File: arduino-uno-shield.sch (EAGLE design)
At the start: 28 parts, among them T1 BC547, T2 BC547, T3 BC547, T4 BC547, T5 BC547, T6 BC547, T7 BC547, U1 SN74HC595N

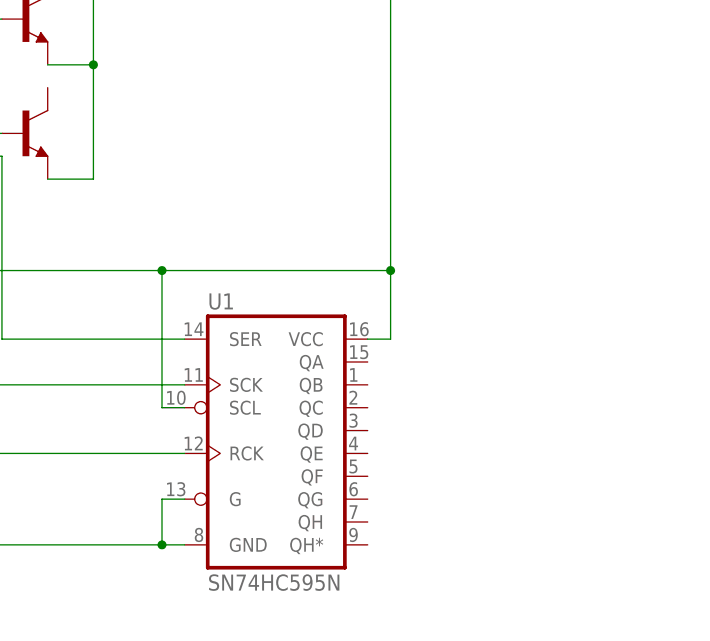
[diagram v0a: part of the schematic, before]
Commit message: Added 6 leds for the clock
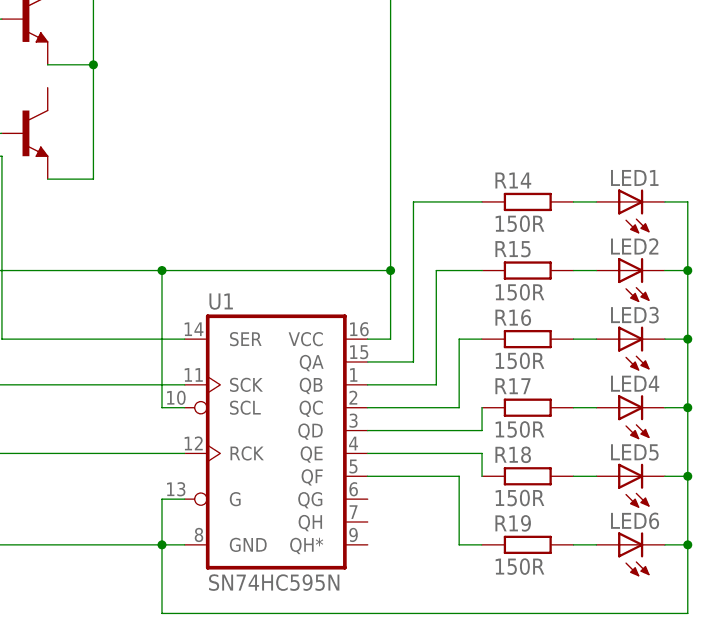
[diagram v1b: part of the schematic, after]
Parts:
- added LED1, LED2, LED3, LED4, LED5, LED6: (no value), led:LED5MM
- added R14, R15, R16, R17, R18, R19: 150R, rcl:R-EU_0204/5
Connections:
- new net N$21: R14.1, U1.QA
- new net N$25: R15.1, U1.QB
- new net N$26: R16.1, U1.QC
- new net N$27: R17.1, U1.QD
- new net N$28: R18.1, U1.QE
- new net N$29: R19.1, U1.QF
- new net N$30: LED1.A, R14.2
- new net N$31: LED2.A, R15.2
- new net N$32: LED3.A, R16.2
- new net N$33: LED4.A, R17.2
- new net N$34: LED5.A, R18.2
- new net N$35: LED6.A, R19.2
- net GND: now also LED1.C, LED2.C, LED3.C, LED4.C, LED5.C, LED6.C
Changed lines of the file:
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@@
 <part name="R13" library="rcl" library_urn="urn:adsk.eagle:library:334" deviceset="R-EU_" device="0204/5" package3d_urn="urn:adsk.eagle:package:23488/1" value="10K"/>
 <part name="U1" library="SparkFun-IC-Logic" deviceset="74*595" device="N" technology="HC" value="SN74HC595N "/>
+<part name="R14" library="rcl" library_urn="urn:adsk.eagle:library:334" deviceset="R-EU_" device="0204/5" package3d_urn="urn:adsk.eagle:package:23488/1" value="150R"/>
+<part name="R15" library="rcl" library_urn="urn:adsk.eagle:library:334" deviceset="R-EU_" device="0204/5" package3d_urn="urn:adsk.eagle:package:23488/1" value="150R"/>
+<part name="R16" library="rcl" library_urn="urn:adsk.eagle:library:334" deviceset="R-EU_" device="0204/5" package3d_urn="urn:adsk.eagle:package:23488/1" value="150R"/>
+<part name="R17" library="rcl" library_urn="urn:adsk.eagle:library:334" deviceset="R-EU_" device="0204/5" package3d_urn="urn:adsk.eagle:package:23488/1" value="150R"/>
+<part name="R18" library="rcl" library_urn="urn:adsk.eagle:library:334" deviceset="R-EU_" device="0204/5" package3d_urn="urn:adsk.eagle:package:23488/1" value="150R"/>
+<part name="R19" library="rcl" library_urn="urn:adsk.eagle:library:334" deviceset="R-EU_" device="0204/5" package3d_urn="urn:adsk.eagle:package:23488/1" value="150R"/>
+<part name="LED1" library="led" library_urn="urn:adsk.eagle:library:259" deviceset="LED" device="5MM" package3d_urn="urn:adsk.eagle:package:15799/2"/>
+<part name="LED2" library="led" library_urn="urn:adsk.eagle:library:259" deviceset="LED" device="5MM" package3d_urn="urn:adsk.eagle:package:15799/2"/>
+<part name="LED3" library="led" library_urn="urn:adsk.eagle:library:259" deviceset="LED" device="5MM" package3d_urn="urn:adsk.eagle:package:15799/2"/>
+<part name="LED4" library="led" library_urn="urn:adsk.eagle:library:259" deviceset="LED" device="5MM" package3d_urn="urn:adsk.eagle:package:15799/2"/>
+<part name="LED5" library="led" library_urn="urn:adsk.eagle:library:259" deviceset="LED" device="5MM" package3d_urn="urn:adsk.eagle:package:15799/2"/>
+<part name="LED6" library="led" library_urn="urn:adsk.eagle:library:259" deviceset="LED" device="5MM" package3d_urn="urn:adsk.eagle:package:15799/2"/>
 </parts>
 <sheets>
@@
 <instance part="R13" gate="G$1" x="58.42" y="-81.28"/>
 <instance part="U1" gate="U1" x="109.22" y="-78.74"/>
+<instance part="R14" gate="G$1" x="139.7" y="-53.34"/>
+<instance part="R15" gate="G$1" x="139.7" y="-60.96"/>
+<instance part="R16" gate="G$1" x="139.7" y="-68.58"/>
+<instance part="R17" gate="G$1" x="139.7" y="-76.2"/>
+<instance part="R18" gate="G$1" x="139.7" y="-83.82"/>
+<instance part="R19" gate="G$1" x="139.7" y="-91.44"/>
+<instance part="LED1" gate="G$1" x="149.86" y="-53.34" rot="R90"/>
+<instance part="LED2" gate="G$1" x="149.86" y="-60.96" rot="R90"/>
+<instance part="LED3" gate="G$1" x="149.86" y="-68.58" rot="R90"/>
+<instance part="LED4" gate="G$1" x="149.86" y="-76.2" rot="R90"/>
+<instance part="LED5" gate="G$1" x="149.86" y="-83.82" rot="R90"/>
+<instance part="LED6" gate="G$1" x="149.86" y="-91.44" rot="R90"/>
 </instances>
 <busses>
@@
 <junction x="99.06" y="-91.44"/>
 <junction x="68.58" y="-91.44"/>
+<pinref part="LED1" gate="G$1" pin="C"/>
+<wire x1="154.94" y1="-53.34" x2="157.48" y2="-53.34" width="0.1524" layer="91"/>
+<wire x1="157.48" y1="-53.34" x2="157.48" y2="-60.96" width="0.1524" layer="91"/>
+<pinref part="LED6" gate="G$1" pin="C"/>
+<wire x1="157.48" y1="-60.96" x2="157.48" y2="-68.58" width="0.1524" layer="91"/>
+<wire x1="157.48" y1="-68.58" x2="157.48" y2="-76.2" width="0.1524" layer="91"/>
+<wire x1="157.48" y1="-76.2" x2="157.48" y2="-83.82" width="0.1524" layer="91"/>
+<wire x1="157.48" y1="-83.82" x2="157.48" y2="-91.44" width="0.1524" layer="91"/>
+<wire x1="157.48" y1="-91.44" x2="154.94" y2="-91.44" width="0.1524" layer="91"/>
+<pinref part="LED5" gate="G$1" pin="C"/>
+<wire x1="154.94" y1="-83.82" x2="157.48" y2="-83.82" width="0.1524" layer="91"/>
+<junction x="157.48" y="-83.82"/>
+<pinref part="LED4" gate="G$1" pin="C"/>
+<wire x1="154.94" y1="-76.2" x2="157.48" y2="-76.2" width="0.1524" layer="91"/>
+<junction x="157.48" y="-76.2"/>
+<pinref part="LED3" gate="G$1" pin="C"/>
+<wire x1="154.94" y1="-68.58" x2="157.48" y2="-68.58" width="0.1524" layer="91"/>
+<junction x="157.48" y="-68.58"/>
+<pinref part="LED2" gate="G$1" pin="C"/>
+<wire x1="154.94" y1="-60.96" x2="157.48" y2="-60.96" width="0.1524" layer="91"/>
+<junction x="157.48" y="-60.96"/>
+<wire x1="157.48" y1="-91.44" x2="157.48" y2="-99.06" width="0.1524" layer="91"/>
+<wire x1="157.48" y1="-99.06" x2="99.06" y2="-99.06" width="0.1524" layer="91"/>
+<junction x="157.48" y="-91.44"/>
+<wire x1="99.06" y1="-99.06" x2="99.06" y2="-91.44" width="0.1524" layer="91"/>
 </segment>
 </net>
@@
 </segment>
 </net>
+<net name="N$21" class="0">
+<segment>
+<pinref part="U1" gate="U1" pin="QA"/>
+<wire x1="121.92" y1="-71.12" x2="127" y2="-71.12" width="0.1524" layer="91"/>
+<wire x1="127" y1="-71.12" x2="127" y2="-53.34" width="0.1524" layer="91"/>
+<pinref part="R14" gate="G$1" pin="1"/>
+<wire x1="127" y1="-53.34" x2="134.62" y2="-53.34" width="0.1524" layer="91"/>
+</segment>
+</net>
+<net name="N$25" class="0">
+<segment>
+<pinref part="R15" gate="G$1" pin="1"/>
+<wire x1="134.62" y1="-60.96" x2="129.54" y2="-60.96" width="0.1524" layer="91"/>
+<wire x1="129.54" y1="-60.96" x2="129.54" y2="-73.66" width="0.1524" layer="91"/>
+<pinref part="U1" gate="U1" pin="QB"/>
+<wire x1="129.54" y1="-73.66" x2="121.92" y2="-73.66" width="0.1524" layer="91"/>
+</segment>
+</net>
+<net name="N$26" class="0">
+<segment>
+<pinref part="U1" gate="U1" pin="QC"/>
+<wire x1="121.92" y1="-76.2" x2="132.08" y2="-76.2" width="0.1524" layer="91"/>
+<wire x1="132.08" y1="-76.2" x2="132.08" y2="-68.58" width="0.1524" layer="91"/>
+<pinref part="R16" gate="G$1" pin="1"/>
+<wire x1="132.08" y1="-68.58" x2="134.62" y2="-68.58" width="0.1524" layer="91"/>
+</segment>
+</net>
+<net name="N$27" class="0">
+<segment>
+<pinref part="U1" gate="U1" pin="QD"/>
+<wire x1="121.92" y1="-78.74" x2="134.62" y2="-78.74" width="0.1524" layer="91"/>
+<wire x1="134.62" y1="-78.74" x2="134.62" y2="-76.2" width="0.1524" layer="91"/>
+<pinref part="R17" gate="G$1" pin="1"/>
+</segment>
+</net>
+<net name="N$28" class="0">
+<segment>
+<pinref part="U1" gate="U1" pin="QE"/>
+<pinref part="R18" gate="G$1" pin="1"/>
+<wire x1="121.92" y1="-81.28" x2="134.62" y2="-81.28" width="0.1524" layer="91"/>
+<wire x1="134.62" y1="-81.28" x2="134.62" y2="-83.82" width="0.1524" layer="91"/>
+</segment>
+</net>
+<net name="N$29" class="0">
+<segment>
+<pinref part="U1" gate="U1" pin="QF"/>
+<wire x1="121.92" y1="-83.82" x2="132.08" y2="-83.82" width="0.1524" layer="91"/>
+<wire x1="132.08" y1="-83.82" x2="132.08" y2="-91.44" width="0.1524" layer="91"/>
+<pinref part="R19" gate="G$1" pin="1"/>
+<wire x1="132.08" y1="-91.44" x2="134.62" y2="-91.44" width="0.1524" layer="91"/>
+</segment>
+</net>
+<net name="N$30" class="0">
+<segment>
+<pinref part="R14" gate="G$1" pin="2"/>
+<pinref part="LED1" gate="G$1" pin="A"/>
+<wire x1="147.32" y1="-53.34" x2="144.78" y2="-53.34" width="0.1524" layer="91"/>
+</segment>
+</net>
+<net name="N$31" class="0">
+<segment>
+<pinref part="R15" gate="G$1" pin="2"/>
+<pinref part="LED2" gate="G$1" pin="A"/>
+<wire x1="147.32" y1="-60.96" x2="144.78" y2="-60.96" width="0.1524" layer="91"/>
+</segment>
+</net>
+<net name="N$32" class="0">
+<segment>
+<pinref part="R16" gate="G$1" pin="2"/>
+<pinref part="LED3" gate="G$1" pin="A"/>
+<wire x1="147.32" y1="-68.58" x2="144.78" y2="-68.58" width="0.1524" layer="91"/>
+</segment>
+</net>
+<net name="N$33" class="0">
+<segment>
+<pinref part="R17" gate="G$1" pin="2"/>
+<pinref part="LED4" gate="G$1" pin="A"/>
+<wire x1="147.32" y1="-76.2" x2="144.78" y2="-76.2" width="0.1524" layer="91"/>
+</segment>
+</net>
+<net name="N$34" class="0">
+<segment>
+<pinref part="R18" gate="G$1" pin="2"/>
+<pinref part="LED5" gate="G$1" pin="A"/>
+<wire x1="147.32" y1="-83.82" x2="144.78" y2="-83.82" width="0.1524" layer="91"/>
+</segment>
+</net>
+<net name="N$35" class="0">
+<segment>
+<pinref part="R19" gate="G$1" pin="2"/>
+<pinref part="LED6" gate="G$1" pin="A"/>
+<wire x1="147.32" y1="-91.44" x2="144.78" y2="-91.44" width="0.1524" layer="91"/>
+</segment>
+</net>

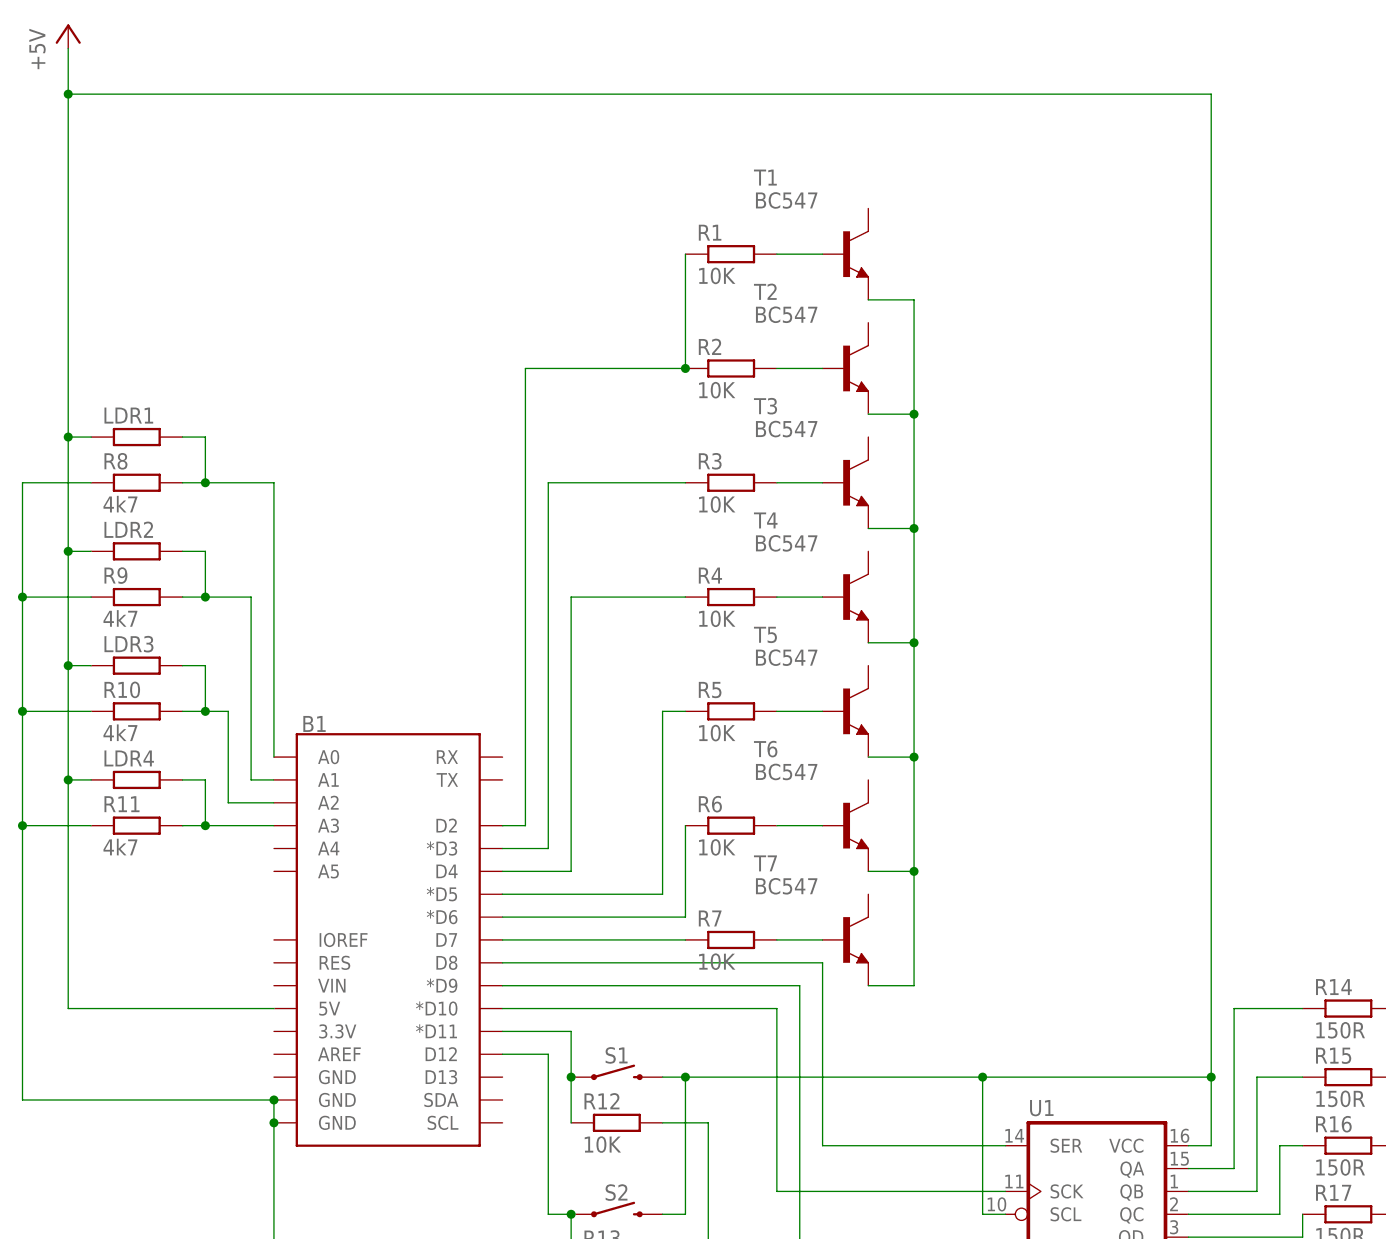
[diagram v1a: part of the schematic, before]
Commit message: added ledstrips
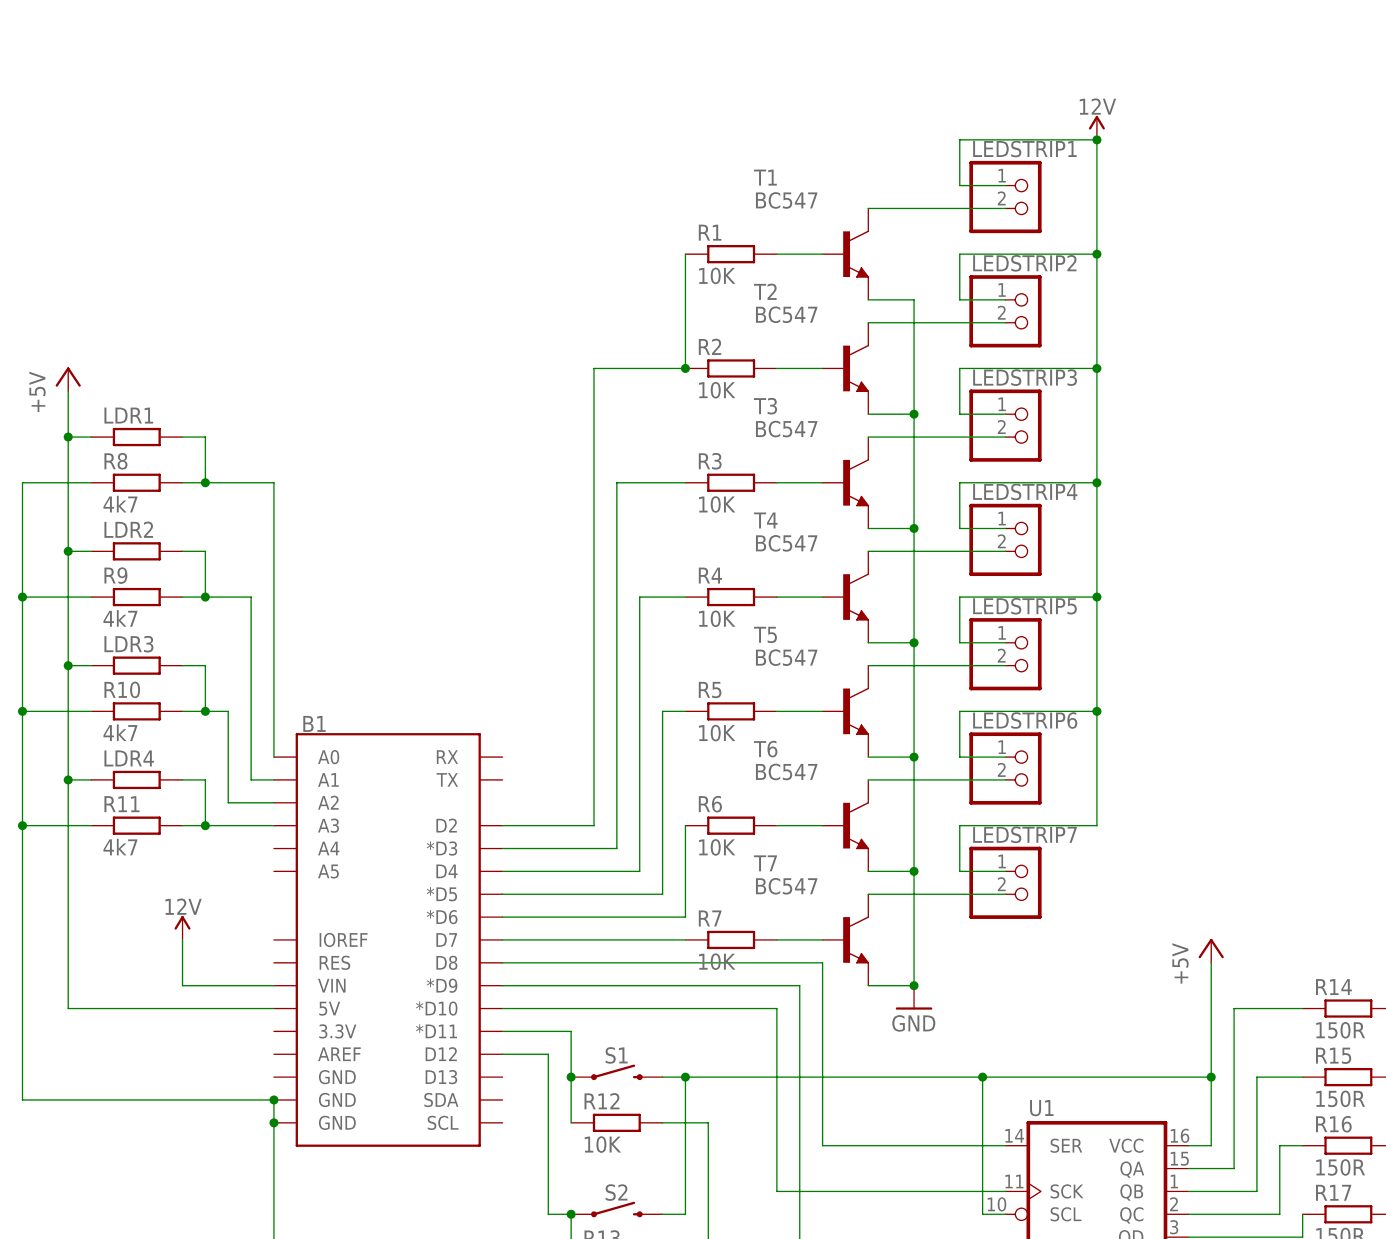
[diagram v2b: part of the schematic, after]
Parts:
- added LEDSTRIP1, LEDSTRIP2, LEDSTRIP3, LEDSTRIP4, LEDSTRIP5, LEDSTRIP6, LEDSTRIP7: (no value), pinhead:PINHD-1X2
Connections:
- new net 12V: B1.VIN, LEDSTRIP1.1, LEDSTRIP2.1, LEDSTRIP3.1, LEDSTRIP4.1, LEDSTRIP5.1, LEDSTRIP6.1, LEDSTRIP7.1
- new net N$36: LEDSTRIP2.2, T2.C
- new net N$37: LEDSTRIP3.2, T3.C
- new net N$38: LEDSTRIP4.2, T4.C
- new net N$39: LEDSTRIP5.2, T5.C
- new net N$40: LEDSTRIP6.2, T6.C
- new net N$41: LEDSTRIP7.2, T7.C
- net GND: now also T1.E, T2.E, T3.E, T4.E, T5.E, T6.E, T7.E
- net N$3: now also LEDSTRIP1.2, T1.C; no longer T1.E, T2.E, T3.E, T4.E, T5.E, T6.E, T7.E
